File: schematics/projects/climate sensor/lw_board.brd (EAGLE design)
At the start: 87.3 x 61 mm, 34 parts, among them J11 J4_FS_2, J3 J2, J7 KF301-5.0, J8 KF301-5.0, Q1 2N3904, Q2 2N3904, Q3 2N3904, Q4 2N3904, Q5 2N3904, Q6 2N3904, U1 BME280, U2 PMS7003, U3 ESP32 DEVKIT WROOM-32D

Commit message: continue work with board
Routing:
- net 3V3: track 163.4 -> 132.1 mm
- net GND: track 251.1 -> 230.3 mm
- net N$26: track 48.1 -> 30.4 mm
- net +5V: track 203.1 -> 191.6 mm
- net N$24: track 29.7 -> 23.9 mm
- net GPIO_RGB_R: track 12.0 -> 6.66 mm
- net I2C_SDA: track 43.5 -> 38.3 mm
- net UART_0_TXD: track 34.5 -> 38.2 mm
- net GPIO_RGB_B: track 12.8 -> 9.94 mm
- net N$27: track 18.9 -> 16.3 mm
- net UART_1_TXD: track 12.8 -> 11.0 mm
- net N$23: track 13.4 -> 11.7 mm
- net I2C_SCL: track 40.3 -> 39.3 mm

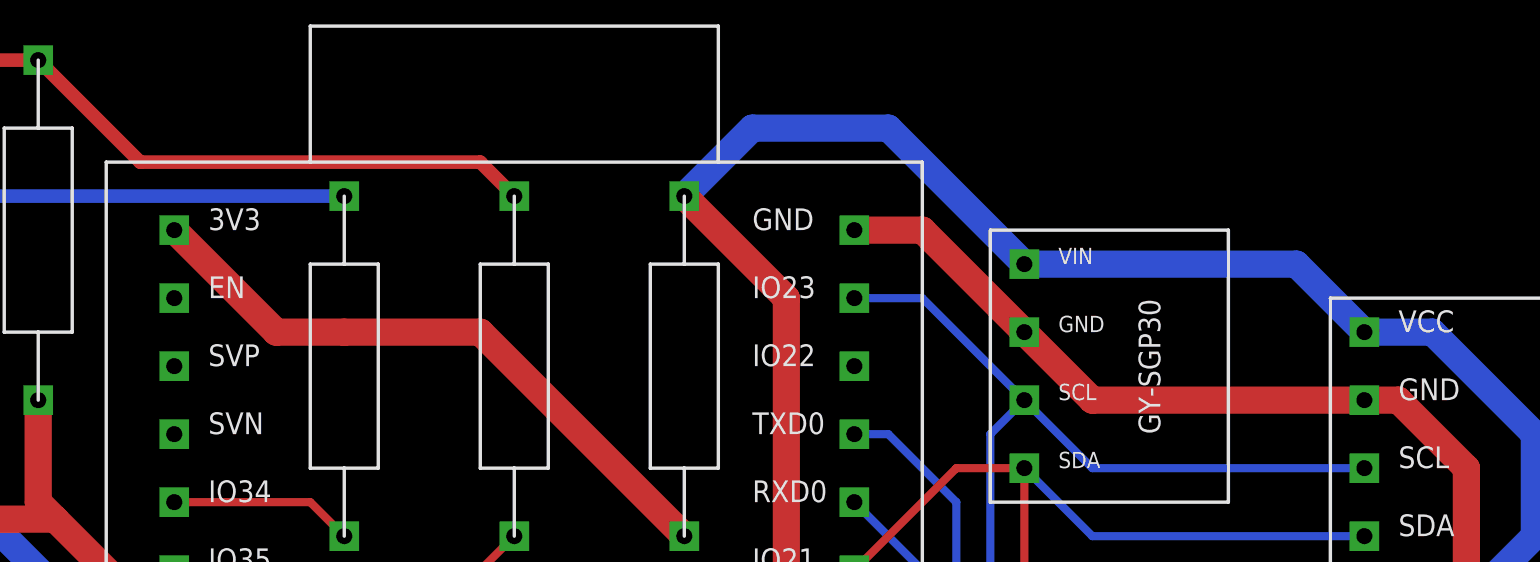
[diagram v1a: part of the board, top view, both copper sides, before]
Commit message: rename elements, optimize board
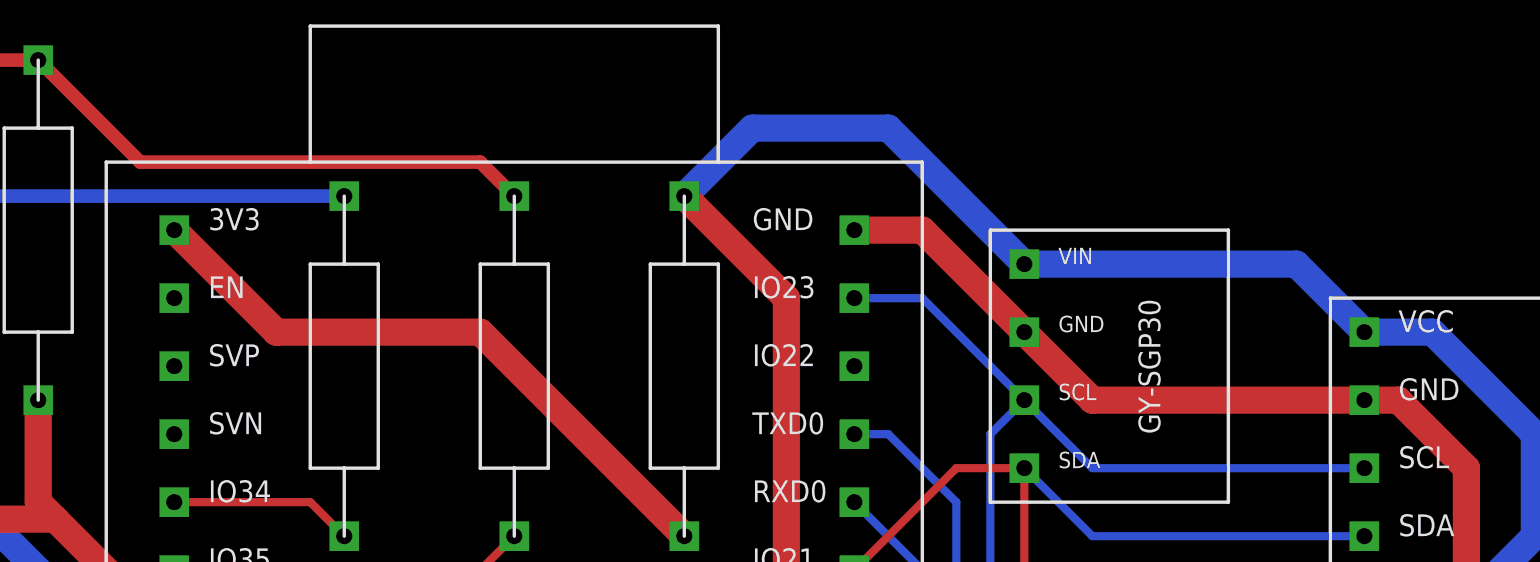
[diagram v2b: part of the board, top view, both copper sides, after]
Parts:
- removed GY_SGP30_1: GY-SGP30, my_devices:GY-SGP30
- added U5: BME280, my_devices:BME280
- R1: value 10K -> 600
- R11: value 30 -> 600
- R12: value 100 -> 600
- R14: value 10K -> 100
- R7: value 600 -> 30
- R8, R9: value 600 -> 10K
- U1: value BME280 -> GY-SGP30; device my_devices:BME280 -> my_devices:GY-SGP30
- U2: value PMS7003 -> ESP32 DEVKIT WROOM-32D; device my_devices:PMS7003_J -> my_devices:ESP32
- U3: value ESP32 DEVKIT WROOM-32D -> PMS7003; device my_devices:ESP32 -> my_devices:PMS7003_J
- moved Q3 43.9 mm to (78.7, 16.5)
- moved Q6 43.9 mm to (38.1, 33.0)
- moved Q4 42.6 mm to (36.8, 14.0), turned to 270 degrees
- moved R10 41.3 mm to (66.0, 20.3)
- moved R11 40.4 mm to (36.8, 19.1), turned to 180 degrees
- moved R8 35.8 mm to (58.4, 20.3)
- moved Q1 34.2 mm to (24.1, 45.7), turned to 0 degrees
- moved U2 33.2 mm to (59.7, 29.2), turned to 0 degrees
- moved U3 33.2 mm to (36.8, 5.08), turned to 90 degrees
- moved R4 31.8 mm to (38.1, 50.8), turned to 270 degrees
- moved R7 31.8 mm to (66.0, 47.0)
- moved R6 30.6 mm to (59.7, 47.0), turned to 270 degrees
- moved R13 29.9 mm to (36.8, 26.7), turned to 180 degrees
- moved R5 29.6 mm to (41.9, 52.1), turned to 270 degrees
- moved R1 28.0 mm to (36.8, 38.1), turned to 0 degrees
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- renumbered J11 to J12, J3 to J10, J7 to J5, J8 to J6, U$11 to U6, U$4 to U4, U$6 to D2
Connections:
- removed net N$23 (its old number): Q3.B, R6.P$2
- new net N$27: Q3.B, R10.P$2
- net +5V: now also Q4.C, Q5.C, Q6.C, R1.P$2, R14.P$1, R4.P$2, U2.+5V, U3.VCC; no longer Q1.C, Q2.C, Q3.C, R10.P$2, R12.P$1, R9.P$2, U2.VCC, U3.+5V
- net 3V3: now also R2.P$2, R5.P$2, R7.P$1, R8.P$1, R9.P$1, U1.VIN, U5.VCC; no longer GY_SGP30_1.VIN, R1.P$1, R11.P$1, R14.P$1, R7.P$2, R8.P$2, U1.VCC
- net GND: now also Q1.E, Q2.E, Q3.E, U5.GND; no longer GY_SGP30_1.GND, Q4.E, Q5.E, Q6.E
- net GPIO_AN_A: now also R3.P$2, U2.IO34; no longer R2.P$2, U3.IO34
- net GPIO_AN_B: now also R6.P$2, U2.IO35; no longer R3.P$2, U3.IO35
- net GPIO_IR: now also R10.P$1, U2.IO2; no longer R13.P$1, U3.IO2
- net GPIO_RGB_B: now also R11.P$1, U2.IO27; no longer R4.P$1, U3.IO27
- net GPIO_RGB_G: now also R12.P$1, U2.IO26; no longer R5.P$1, U3.IO26
- net GPIO_RGB_R: now also R13.P$1, U2.IO25; no longer R6.P$1, U3.IO25
- net GPIO_TS: now also U2.IO4; no longer U3.IO4
- net I2C_SCL: now also U2.IO23, U5.SCL; no longer GY_SGP30_1.SCL, U3.IO23
- net I2C_SDA: now also U2.IO21, U5.SDA; no longer GY_SGP30_1.SDA, U3.IO21
- net N$1: now also Q4.E; no longer Q1.E
- net N$11: now also U2.IO32; no longer U3.IO32
- net N$2: now also Q5.E; no longer Q2.E
- net N$21: now also Q4.B, R11.P$2; no longer Q1.B, R4.P$2
- net N$22: now also Q5.B, R12.P$2; no longer Q2.B, R5.P$2
- net N$24: now also R7.P$2, U2.3V3; no longer R11.P$2, U3.3V3
- net N$25: now also Q3.C; no longer Q6.C
- net N$26: now also R14.P$2; no longer R12.P$2
- net N$28: now also R9.P$2, U3.SET; no longer R14.P$2, U2.SET
- net N$3: now also Q6.E; no longer Q3.E
- net N$4: now also Q2.B, R4.P$1; no longer Q4.B, R10.P$1
- net N$5: now also Q1.B, R1.P$1; no longer Q5.B, R9.P$1
- net N$6: now also Q1.C, R3.P$1; no longer Q5.C, R7.P$1
- net N$7: now also Q2.C, R5.P$1, R6.P$1; no longer Q4.C, R3.P$1, R8.P$1
- net N$8: now also R8.P$2, U3.RESET; no longer R1.P$2, U2.RESET
- net UART_0_RXD: now also U2.RXD; no longer U3.RXD
- net UART_0_TXD: now also U2.TXD0; no longer U3.TXD0
- net UART_1_RXD: now also U2.SD2, U3.TXD; no longer U2.TXD, U3.SD2
- net UART_1_TXD: now also U2.SD3, U3.RXD; no longer U2.RXD, U3.SD3
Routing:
- net N$27: track 0.00 -> 16.3 mm
- net N$23 (its old number): track 11.7 -> 0.00 mm
- net N$23: track 16.3 -> 11.7 mm
